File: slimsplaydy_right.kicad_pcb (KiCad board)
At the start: 2 copper layers, 117.1 x 87.4 mm, 24 parts

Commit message: Finish layout, schematic, routing.
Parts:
- removed B1: , E73:SW_TACT_ALPS_SKQGABE010
- removed T1: , E73:SPDT_C128955
- removed XX1, XX2: , Pad_Single
- removed XX3: , Battery_301230
- added MAG1: , magsafe, B.Cu at (179.9, -32.5)
- added MH1: , ceoloide:mounting_hole_npth, F.Cu at (133.1, 28.8)
- added MH10: , ceoloide:mounting_hole_npth, F.Cu at (195.9, -8.95)
- added MH11: , ceoloide:mounting_hole_npth, F.Cu at (216.9, 11.5)
- added MH12: , ceoloide:mounting_hole_npth, F.Cu at (232.9, 11.9)
- added MH13: , ceoloide:mounting_hole_npth, F.Cu at (240.9, -42.7)
- added MH14: , ceoloide:mounting_hole_npth, F.Cu at (222.0, -51.8)
- added MH15: , ceoloide:mounting_hole_npth, F.Cu at (163.9, -60.5)
- added MH2: , ceoloide:mounting_hole_npth, F.Cu at (238.0, -15.3)
- added MH3: , ceoloide:mounting_hole_npth, F.Cu at (189.9, -64.8)
- added MH4: , ceoloide:mounting_hole_npth, F.Cu at (147.9, -57.8)
- added MH5: , ceoloide:mounting_hole_npth, F.Cu at (123.4, -55.5)
- added MH6: , ceoloide:mounting_hole_npth, F.Cu at (134.9, -21.5)
- added MH7: , ceoloide:mounting_hole_npth, F.Cu at (142.4, 0.55)
- added MH8: , ceoloide:mounting_hole_npth, F.Cu at (123.9, 8.55)
- added MH9: , ceoloide:mounting_hole_npth, F.Cu at (165.0, 15.1)
- added PWR1: , ceoloide:power_switch_smd_side, F.Cu at (123.2, -1.45)
- added RST1: , ceoloide:reset_switch_smd_side, F.Cu at (123.9, -12.5)
- CONN1: footprint ceoloide:battery_connector_molex_pico_ezmate_1x02 -> Molex_Pico_EZMate_Plus_1x02
- S1, S10, S11, S12, S13, S14, S15, S16, S17, S2, S3, S4, S5, S6, S7, S8, S9: footprint CPG1316S01D02_mikeholscher -> PG1316S
- moved CONN1 201.5 mm to (184.9, -8.45), turned to 0 degrees
- moved S6 181.1 mm to (209.8, -47.4), turned to -3 degrees
- moved S5 180.5 mm to (208.9, -30.5), turned to -3 degrees
- moved MCU1 180.1 mm to (134.9, -41.5)
- moved S9 180.0 mm to (189.9, -54.5), turned to 0 degrees
- moved S4 179.9 mm to (208.0, -13.5), turned to -3 degrees
- moved S8 179.5 mm to (189.9, -37.5), turned to 0 degrees
- moved S3 179.1 mm to (229.7, -33.7), turned to -8 degrees
- moved S7 178.9 mm to (189.9, -20.5), turned to 0 degrees
- moved S2 178.7 mm to (227.4, -16.8), turned to -8 degrees
- moved S1 178.2 mm to (225.0, 0.00), turned to -8 degrees
- moved S17 178.1 mm to (136.5, 14.7)
- moved S12 177.7 mm to (171.9, -49.5), turned to 0 degrees
- moved S11 177.5 mm to (171.9, -32.5), turned to 0 degrees
- moved S10 177.4 mm to (171.9, -15.5), turned to 0 degrees
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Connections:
- MCU1 pad 1: mirror_hand_middle_top -> mirror_finger_inner_home
- MCU1 pad 10: mirror_hand_inner_home -> mirror_finger_pinky_top
- MCU1 pad 11: mirror_hand_ring_home -> mirror_thumb_tucky_fan
- MCU1 pad 12: mirror_hand_pinky_home -> mirror_thumb_reachy_fan
- MCU1 pad 13: mirror_hand_pinky_bottom -> mirror_finger_index_home
- MCU1 pad 14: mirror_hand_middle_bottom -> mirror_finger_middle_home
- MCU1 pad 15: mirror_hand_index_bottom -> mirror_finger_ring_home
- MCU1 pad 16: mirror_hand_inner_bottom -> mirror_finger_pinky_home
- MCU1 pad 17: mirror_hand_ring_bottom -> mirror_finger_ring_top
- MCU1 pad 18: mirror_thumb_near_fan -> mirror_finger_middle_top
- MCU1 pad 19: mirror_thumb_far_fan -> mirror_finger_index_top
- MCU1 pad 2: mirror_hand_index_top -> D0
- MCU1 pad 20: D21 -> mirror_finger_inner_top
- MCU1 pad 24: BAT -> RAW
- MCU1 pad 5: mirror_hand_inner_top -> mirror_finger_pinky_bottom
- MCU1 pad 6: mirror_hand_ring_top -> mirror_finger_ring_bottom
- MCU1 pad 7: mirror_hand_pinky_top -> mirror_finger_middle_bottom
- MCU1 pad 8: mirror_hand_middle_home -> mirror_finger_index_bottom
- MCU1 pad 9: mirror_hand_index_home -> mirror_finger_inner_bottom
- S1 pad 1: mirror_hand_pinky_bottom -> mirror_finger_pinky_bottom
- S1 pad 3: (no net) -> GND
- S10 pad 1: mirror_hand_index_bottom -> mirror_finger_index_bottom
- S10 pad 3: (no net) -> GND
- S11 pad 1: mirror_hand_index_home -> mirror_finger_index_home
- S11 pad 3: (no net) -> GND
- S12 pad 1: mirror_hand_index_top -> mirror_finger_index_top
- S12 pad 3: (no net) -> GND
- S13 pad 1: mirror_hand_inner_bottom -> mirror_finger_inner_bottom
- S13 pad 3: (no net) -> GND
- S14 pad 1: mirror_hand_inner_home -> mirror_finger_inner_home
- S14 pad 3: (no net) -> GND
- S15 pad 1: mirror_hand_inner_top -> mirror_finger_inner_top
- S15 pad 3: (no net) -> GND
- S16 pad 1: mirror_thumb_near_fan -> mirror_thumb_tucky_fan
- S16 pad 3: (no net) -> GND
- S17 pad 1: mirror_thumb_far_fan -> mirror_thumb_reachy_fan
- S17 pad 3: (no net) -> GND
- S2 pad 1: mirror_hand_pinky_home -> mirror_finger_pinky_home
- S2 pad 3: (no net) -> GND
- S3 pad 1: mirror_hand_pinky_top -> mirror_finger_pinky_top
- S3 pad 3: (no net) -> GND
- S4 pad 1: mirror_hand_ring_bottom -> mirror_finger_ring_bottom
- S4 pad 3: (no net) -> GND
- S5 pad 1: mirror_hand_ring_home -> mirror_finger_ring_home
- S5 pad 3: (no net) -> GND
- S6 pad 1: mirror_hand_ring_top -> mirror_finger_ring_top
- S6 pad 3: (no net) -> GND
- S7 pad 1: mirror_hand_middle_bottom -> mirror_finger_middle_bottom
- S7 pad 3: (no net) -> GND
- S8 pad 1: mirror_hand_middle_home -> mirror_finger_middle_home
- S8 pad 3: (no net) -> GND
- S9 pad 1: mirror_hand_middle_top -> mirror_finger_middle_top
- S9 pad 3: (no net) -> GND
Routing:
- net BAT: track 160.1 -> 0.00 mm, vias 2 -> 0
- net RST: track 141.1 -> 0.00 mm, vias 2 -> 0
- net mirror_hand_pinky_bottom: track 104.6 -> 0.00 mm, vias 2 -> 0
- net mirror_hand_ring_bottom: track 100.1 -> 0.00 mm, vias 2 -> 0
- net mirror_hand_pinky_top: track 86.6 -> 0.00 mm, vias 2 -> 0
- net mirror_hand_pinky_home: track 85.4 -> 0.00 mm, vias 2 -> 0
- net mirror_hand_middle_bottom: track 69.2 -> 0.00 mm, vias 2 -> 0
- net mirror_thumb_near_fan: track 66.6 -> 0.00 mm, vias 2 -> 0
- net mirror_hand_ring_top: track 65.4 -> 0.00 mm, vias 2 -> 0
- net mirror_hand_ring_home: track 63.4 -> 0.00 mm, vias 2 -> 0
- net mirror_thumb_far_fan: track 63.1 -> 0.00 mm, vias 2 -> 0
- net mirror_hand_index_bottom: track 55.0 -> 0.00 mm, vias 2 -> 0
- net mirror_hand_middle_top: track 48.6 -> 0.00 mm, vias 2 -> 0
- net mirror_hand_middle_home: track 46.0 -> 0.00 mm, vias 2 -> 0
- net mirror_hand_inner_bottom: track 43.0 -> 0.00 mm, vias 2 -> 0
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- removed copper zone on F.Cu, net GND
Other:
- board size 117.1 x 87.4 mm -> 122.6 x 97.5 mm

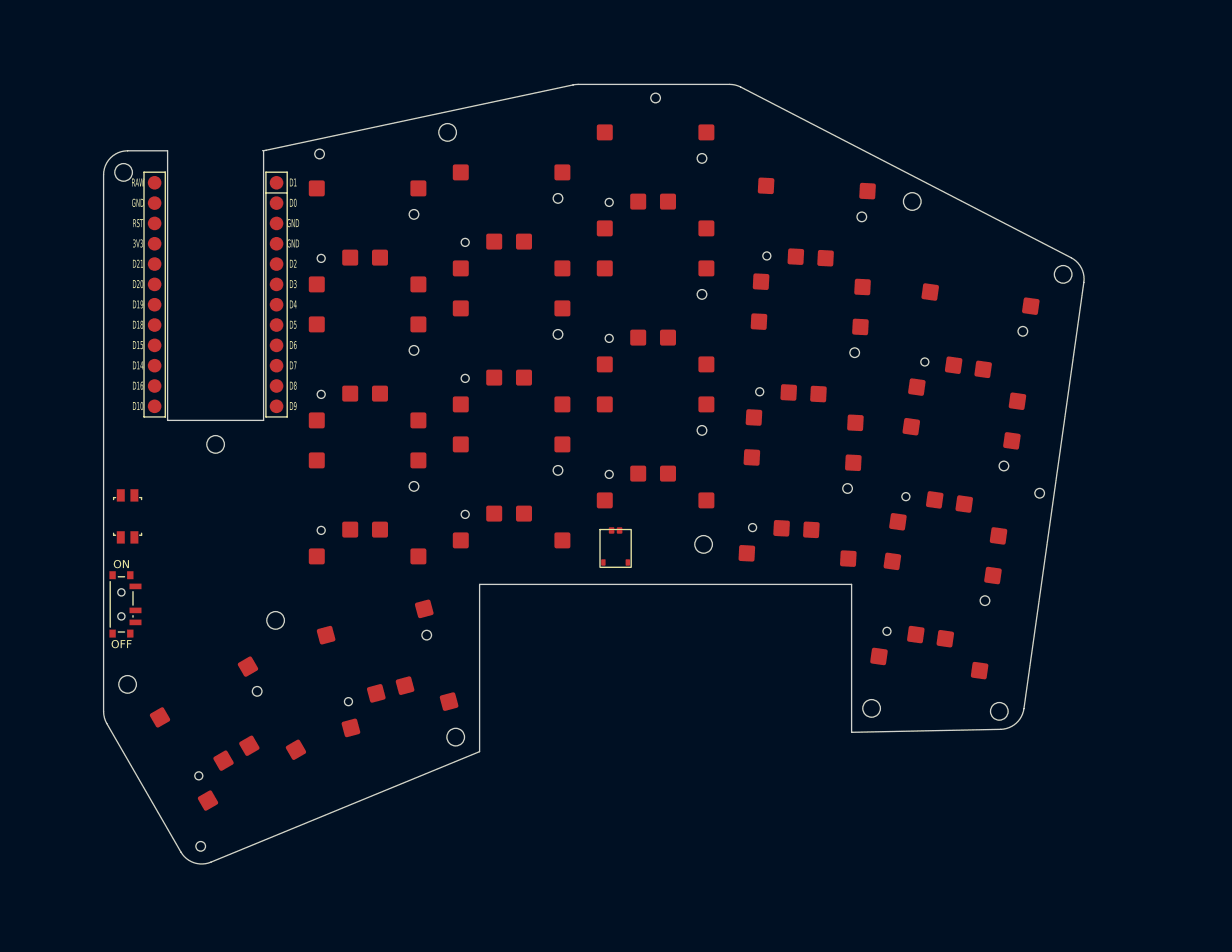
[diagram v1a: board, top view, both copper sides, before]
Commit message: First draft routing for right side. Reeeeaaally ugly.
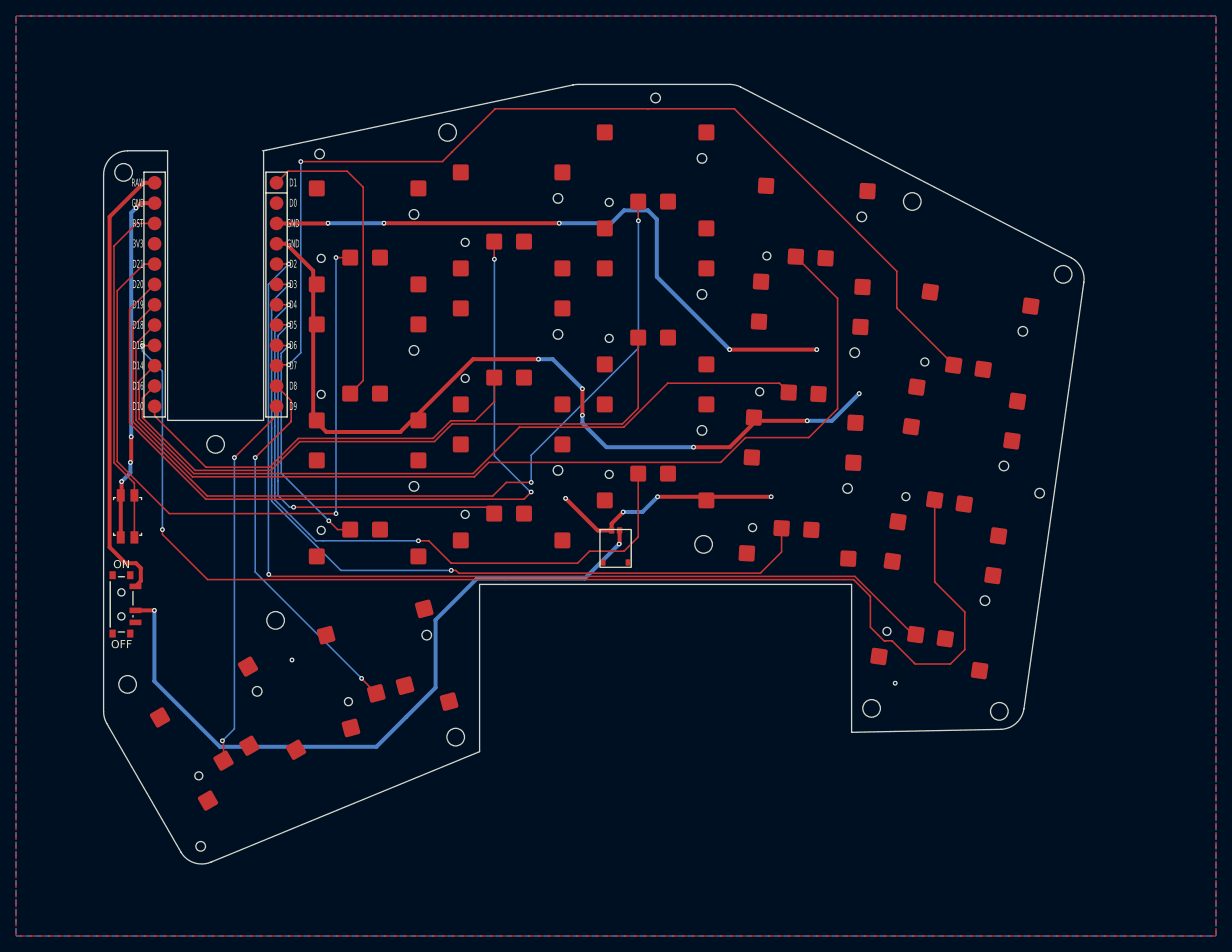
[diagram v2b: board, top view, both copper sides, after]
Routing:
- net GND: track 0.00 -> 260.8 mm, vias 0 -> 21
- net mirror_finger_pinky_home: track 0.00 -> 156.5 mm, vias 0 -> 2
- net mirror_finger_ring_top: track 0.00 -> 128.2 mm
- net mirror_finger_pinky_top: track 0.00 -> 127.9 mm, vias 0 -> 2
- net mirror_finger_pinky_bottom: track 0.00 -> 125.4 mm, vias 0 -> 2
- net mirror_finger_middle_top: track 0.00 -> 110.8 mm, vias 0 -> 2
- net mirror_finger_index_top: track 0.00 -> 106.4 mm, vias 0 -> 2
- net mirror_finger_ring_bottom: track 0.00 -> 101.0 mm, vias 0 -> 2
- net mirror_finger_ring_home: track 0.00 -> 96.6 mm
- net mirror_finger_inner_top: track 0.00 -> 91.2 mm, vias 0 -> 2
- net BAT_P: track 0.00 -> 89.9 mm, vias 0 -> 2
- net mirror_finger_middle_bottom: track 0.00 -> 84.6 mm, vias 0 -> 2
- net mirror_finger_middle_home: track 0.00 -> 81.3 mm
- net RAW: track 0.00 -> 56.2 mm
- net mirror_finger_index_home: track 0.00 -> 52.7 mm
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- added copper zone on B.Cu, net GND
- added copper zone on F.Cu, net GND

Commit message: Fix MCU slots. Fillet outline. Reroute both sides. Re-re-reroute both sides.
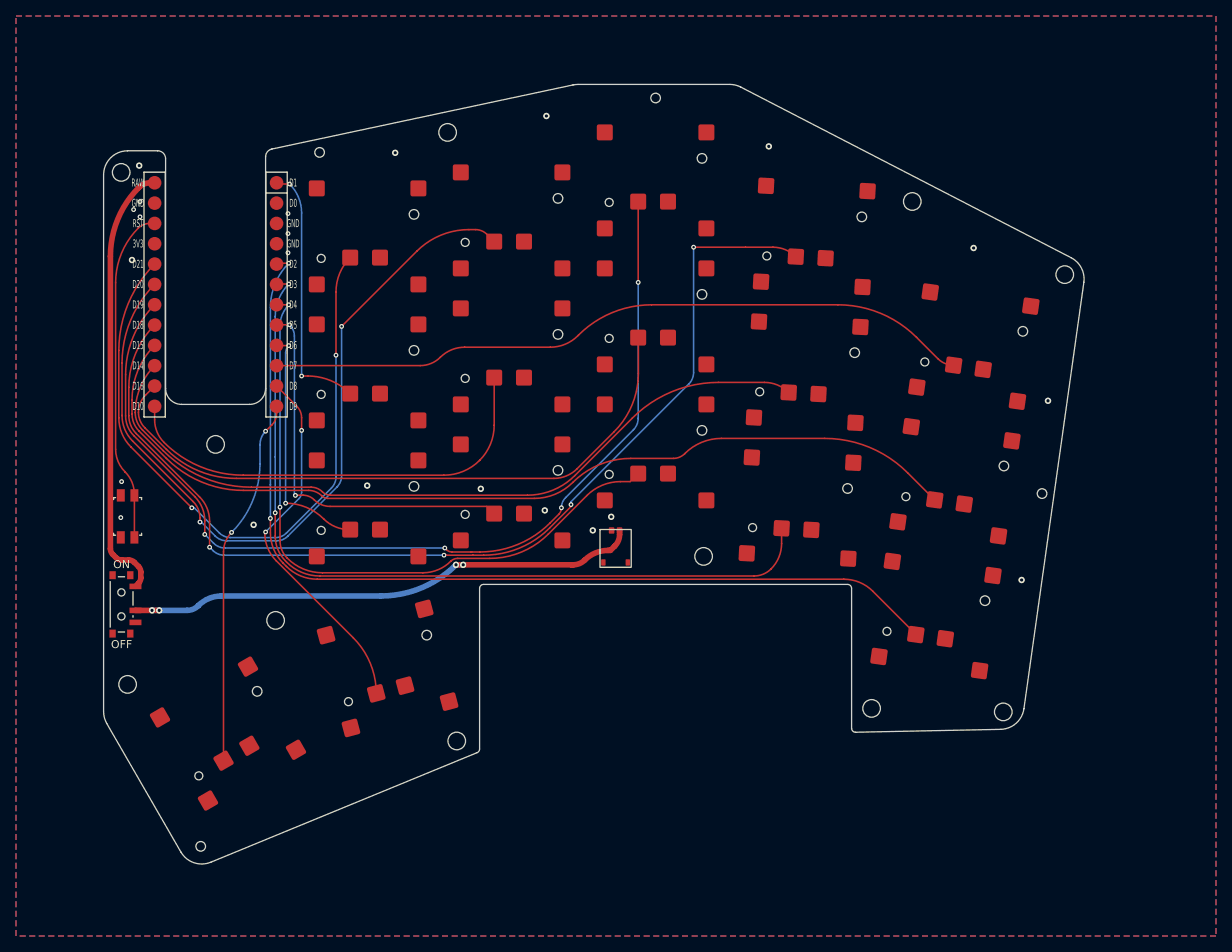
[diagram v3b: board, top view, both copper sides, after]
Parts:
- CONN1: value (none) -> Battery Connector
- MCU1: value (none) -> nice_nano
- PWR1: value (none) -> Power SW
- RST1: value (none) -> Reset SW
- S1, S10, S11, S12, S13, S14, S15, S16, S17, S2, S3, S4, S5, S6, S7, S8, S9: value (none) -> PG1316S
- moved MH10 1.50 mm to (195.9, -7.45)
- moved MH9 0.50 mm to (165.1, 15.6)
- moved MH12 0.50 mm to (233.4, 12.0)
- moved MH5 0.30 mm to (123.1, -55.5)
- moved MH2 0.30 mm to (238.3, -15.3)
- moved MH4 0.20 mm to (147.9, -58.0)
- moved MH13 0.20 mm to (241.1, -42.7)
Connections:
- MCU1 pad 2: D0 -> unconnected-(MCU1-P0.08-Pad2)
- MCU1 pad 21: 3V3 -> unconnected-(MCU1-3V3-Pad21)
- PWR1 pad 3: (no net) -> unconnected-(PWR1-C-Pad3)
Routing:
- net GND: track 260.8 -> 0.00 mm, vias 21 -> 22
- net mirror_finger_pinky_top: track 127.9 -> 88.9 mm, vias 2 -> 0
- net mirror_finger_pinky_home: track 156.5 -> 118.1 mm, vias 2 -> 0
- net BAT_P: track 89.9 -> 65.9 mm, vias 2 -> 4
- net mirror_finger_middle_top: track 110.8 -> 122.7 mm, vias 2 -> 4
- net mirror_finger_index_top: track 106.4 -> 99.5 mm
- net mirror_finger_inner_home: track 38.7 -> 32.7 mm, vias 0 -> 2
- net mirror_finger_inner_top: track 91.2 -> 85.9 mm
- net mirror_finger_index_home: track 52.7 -> 56.5 mm
- net mirror_finger_ring_top: track 128.2 -> 131.6 mm, vias 0 -> 4
- net mirror_finger_pinky_bottom: track 125.4 -> 122.4 mm
- net mirror_finger_ring_bottom: track 101.0 -> 103.7 mm
- net mirror_finger_index_bottom: track 51.4 -> 48.8 mm
- net mirror_finger_middle_bottom: track 84.6 -> 82.1 mm
- net RST: track 43.7 -> 42.1 mm
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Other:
- outline, holes or cut-outs redrawn

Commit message: Add production files.
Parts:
- moved MCU1 0.20 mm to (134.9, -41.7)
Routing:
- net mirror_finger_ring_top: track 131.6 -> 144.7 mm, vias 4 -> 2
- net mirror_finger_index_top: track 99.5 -> 110.3 mm
- net mirror_finger_inner_top: track 85.9 -> 94.3 mm
- net mirror_finger_middle_bottom: track 82.1 -> 89.8 mm
- net mirror_finger_middle_home: track 81.6 -> 78.5 mm
- net mirror_finger_pinky_home: track 118.1 -> 121.1 mm
- net mirror_finger_middle_top: track 122.7 -> 125.6 mm, vias 4 -> 2
- net mirror_thumb_tucky_fan: track 46.5 -> 48.8 mm
- net mirror_finger_index_bottom: track 48.8 -> 51.0 mm
- net mirror_finger_ring_home: track 97.1 -> 99.0 mm
- net BAT_P: track 65.9 -> 67.7 mm, vias 4 -> 6
- net mirror_finger_pinky_bottom: track 122.4 -> 123.9 mm
- net mirror_finger_index_home: track 56.5 -> 58.0 mm
- net mirror_finger_pinky_top: track 88.9 -> 89.9 mm
- net mirror_finger_inner_bottom: track 30.2 -> 31.1 mm
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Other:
- outline, holes or cut-outs redrawn

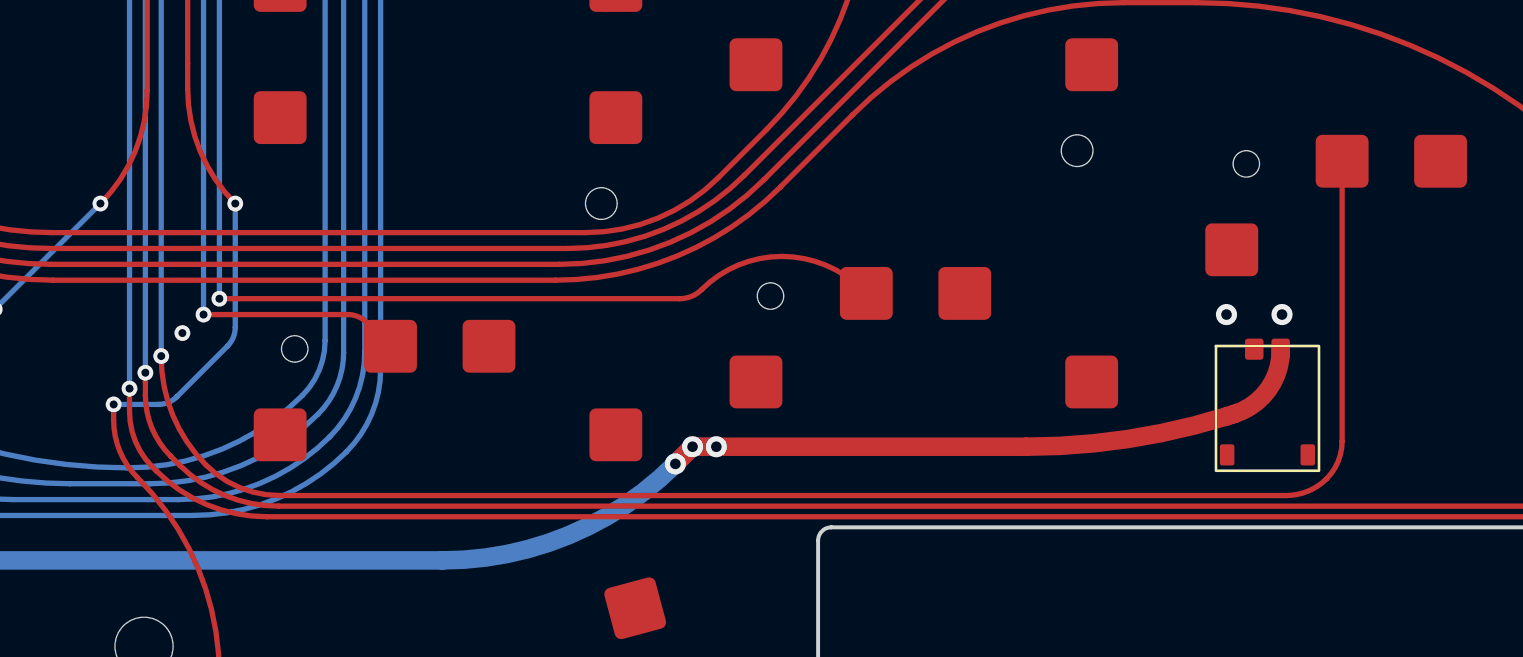
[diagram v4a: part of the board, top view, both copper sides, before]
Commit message: Cleanup ergogen and other from ezmate 1.0mm -> 1.2mm swap
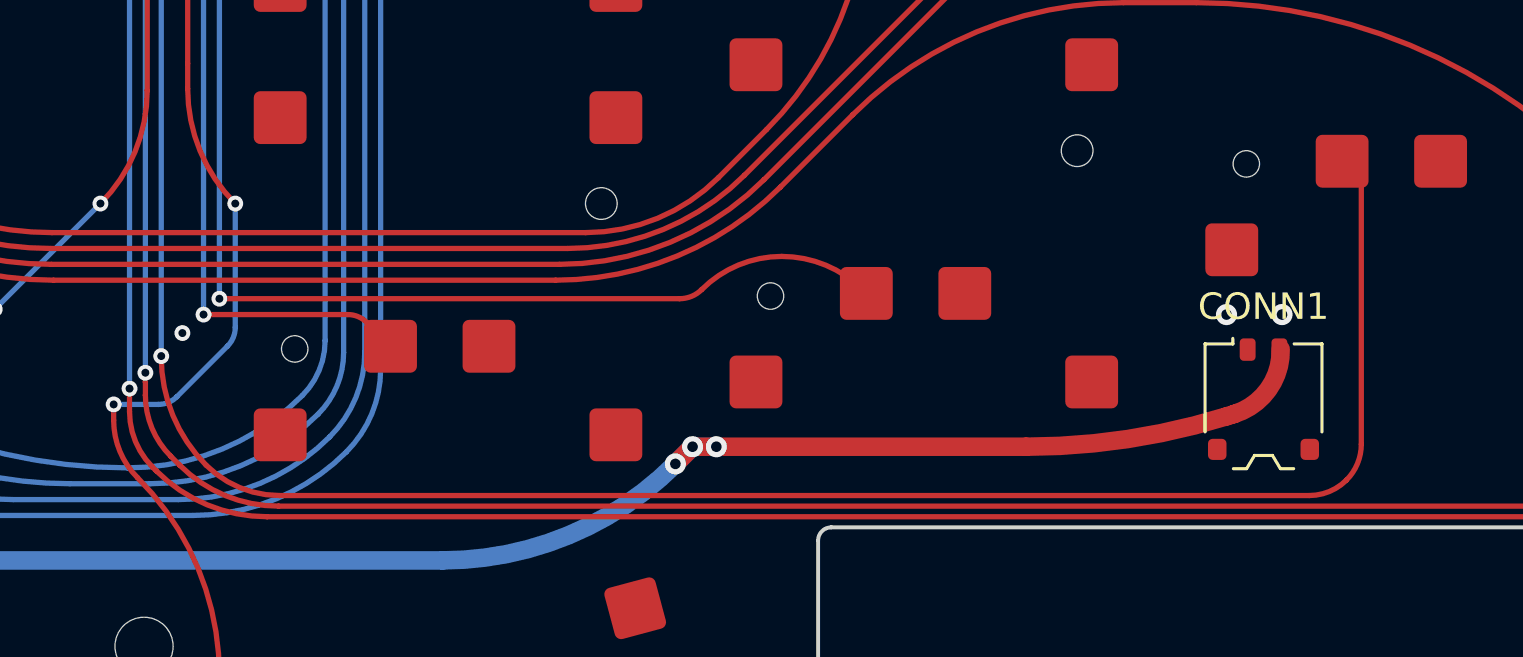
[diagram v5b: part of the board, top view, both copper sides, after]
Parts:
- CONN1: footprint Molex_Pico_EZMate_Plus_1x02 -> Connector_Molex:Molex_Pico-EZmate_78171-0002_1x02-1MP_P1.20mm_Vertical
- moved CONN1 0.38 mm to (184.8, -8.80)
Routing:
- net mirror_finger_middle_bottom: track 89.8 -> 90.9 mm
